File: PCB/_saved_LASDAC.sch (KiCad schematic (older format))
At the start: 21 parts, among them P1 USB_B, P2 CONN_01X25, U1 Mounting_Hole, U2 Mounting_Hole, U3 Mounting_Hole, U4 Mounting_Hole

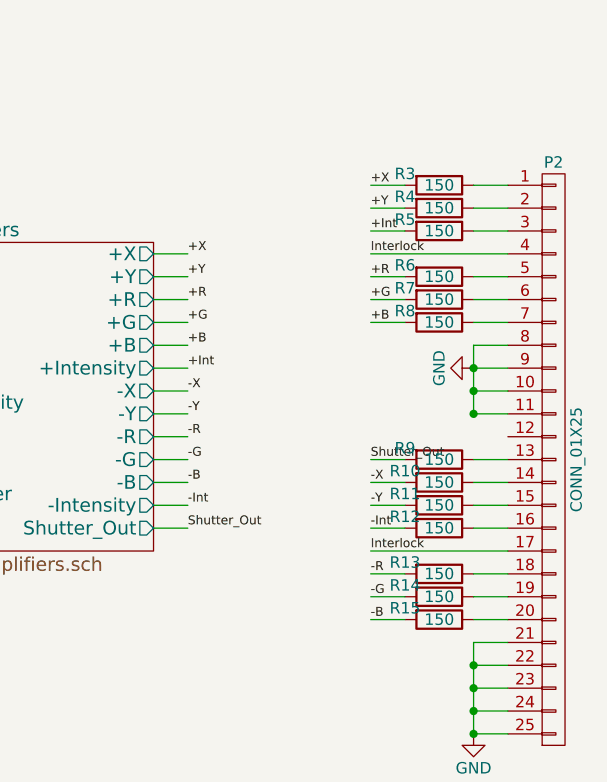
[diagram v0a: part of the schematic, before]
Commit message: Generated BOM, fixed component names in schematic
Changed component names on output resistors and status LED to match that
in PCB
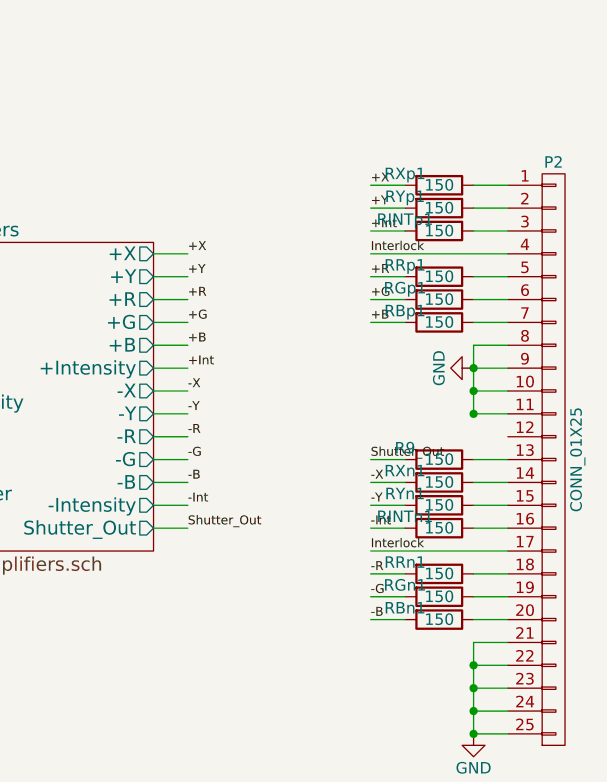
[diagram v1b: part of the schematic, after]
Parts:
- renumbered R15 to RBn1, R8 to RBp1, R14 to RGn1, R7 to RGp1, R12 to RINTn1, R5 to RINTp1, R13 to RRn1, R6 to RRp1, R10 to RXn1, R3 to RXp1, R11 to RYn1, R4 to RYp1
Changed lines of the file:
@@
 $EndComp
 $Comp
-L R R3
+L R RXp1
 U 1 1 56C38472
 P 10600 1600
-F 0 "R3" V 10550 1450 50  0000 C CNN
+F 0 "RXp1" V 10550 1450 50  0000 C CNN
 F 1 "150" V 10600 1600 50  0000 C CNN
 F 2 "Resistors_SMD:R_0805" V 10530 1600 50  0001 C CNN
@@
 $EndComp
 $Comp
-L R R4
+L R RYp1
 U 1 1 56C39BBD
 P 10600 1700
-F 0 "R4" V 10550 1550 50  0000 C CNN
+F 0 "RYp1" V 10550 1550 50  0000 C CNN
 F 1 "150" V 10600 1700 50  0000 C CNN
 F 2 "Resistors_SMD:R_0805" V 10530 1700 50  0001 C CNN
@@
 $EndComp
 $Comp
-L R R6
+L R RRp1
 U 1 1 56C39CF9
 P 10600 2000
-F 0 "R6" V 10550 1850 50  0000 C CNN
+F 0 "RRp1" V 10550 1850 50  0000 C CNN
 F 1 "150" V 10600 2000 50  0000 C CNN
 F 2 "Resistors_SMD:R_0805" V 10530 2000 50  0001 C CNN
@@
 $EndComp
 $Comp
-L R R7
+L R RGp1
 U 1 1 56C3B39A
 P 10600 2100
-F 0 "R7" V 10550 1950 50  0000 C CNN
+F 0 "RGp1" V 10550 1950 50  0000 C CNN
 F 1 "150" V 10600 2100 50  0000 C CNN
 F 2 "Resistors_SMD:R_0805" V 10530 2100 50  0001 C CNN
@@
 $EndComp
 $Comp
-L R R8
+L R RBp1
 U 1 1 56C3B4DC
 P 10600 2200
-F 0 "R8" V 10550 2050 50  0000 C CNN
+F 0 "RBp1" V 10550 2050 50  0000 C CNN
 F 1 "150" V 10600 2200 50  0000 C CNN
 F 2 "Resistors_SMD:R_0805" V 10530 2200 50  0001 C CNN
@@
 $EndComp
 $Comp
-L R R10
+L R RXn1
 U 1 1 56C3BB53
 P 10600 2900
-F 0 "R10" V 10550 2750 50  0000 C CNN
+F 0 "RXn1" V 10550 2750 50  0000 C CNN
 F 1 "150" V 10600 2900 50  0000 C CNN
 F 2 "Resistors_SMD:R_0805" V 10530 2900 50  0001 C CNN
@@
 $EndComp
 $Comp
-L R R11
+L R RYn1
 U 1 1 56C3BCAF
 P 10600 3000
-F 0 "R11" V 10550 2850 50  0000 C CNN
+F 0 "RYn1" V 10550 2850 50  0000 C CNN
 F 1 "150" V 10600 3000 50  0000 C CNN
 F 2 "Resistors_SMD:R_0805" V 10530 3000 50  0001 C CNN
@@
 $EndComp
 $Comp
-L R R13
+L R RRn1
 U 1 1 56C3C072
 P 10600 3300
-F 0 "R13" V 10550 3150 50  0000 C CNN
+F 0 "RRn1" V 10550 3150 50  0000 C CNN
 F 1 "150" V 10600 3300 50  0000 C CNN
 F 2 "Resistors_SMD:R_0805" V 10530 3300 50  0001 C CNN
@@
 $EndComp
 $Comp
-L R R14
+L R RGn1
 U 1 1 56C3C1D4
 P 10600 3400
-F 0 "R14" V 10550 3250 50  0000 C CNN
+F 0 "RGn1" V 10550 3250 50  0000 C CNN
 F 1 "150" V 10600 3400 50  0000 C CNN
 F 2 "Resistors_SMD:R_0805" V 10530 3400 50  0001 C CNN
@@
 $EndComp
 $Comp
-L R R15
+L R RBn1
 U 1 1 56C3C331
 P 10600 3500
-F 0 "R15" V 10550 3350 50  0000 C CNN
+F 0 "RBn1" V 10550 3350 50  0000 C CNN
 F 1 "150" V 10600 3500 50  0000 C CNN
 F 2 "Resistors_SMD:R_0805" V 10530 3500 50  0001 C CNN
@@
 $EndComp
 $Comp
-L R R5
+L R RINTp1
 U 1 1 56C33D0E
 P 10600 1800
-F 0 "R5" V 10550 1650 50  0000 C CNN
+F 0 "RINTp1" V 10550 1650 50  0000 C CNN
 F 1 "150" V 10600 1800 50  0000 C CNN
 F 2 "Resistors_SMD:R_0805" V 10530 1800 50  0001 C CNN
@@
 $EndComp
 $Comp
-L R R12
+L R RINTn1
 U 1 1 56C341ED
 P 10600 3100
-F 0 "R12" V 10550 2950 50  0000 C CNN
+F 0 "RINTn1" V 10550 2950 50  0000 C CNN
 F 1 "150" V 10600 3100 50  0000 C CNN
 F 2 "Resistors_SMD:R_0805" V 10530 3100 50  0001 C CNN
